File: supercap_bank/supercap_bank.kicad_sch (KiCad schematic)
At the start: 0 parts

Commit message: Update KiCad project files
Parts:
- added C20, C21, C22, C23: 10 F, capacitor_footprints:C_197x394_H31_5_5_0x10Metric, symbol CAPACITORS_HV_DATA_BASE:C_HV1030-2R7106-R
- added FID1, FID2, FID3: Fiducial, no_components_footprints:Fiducial_0.5mm_Mask1mm, symbol UNITED_NO_COMPONENTS_DATA_BASE:Fiducial
- added J10, J6, J7, J8, J9: FTSH-102-04-L-DH, connector_footprints:FTSH-102-04-L-DH, symbol CONNECTORS_FTSH-1xx-04-L-DH_DATA_BASE:J_FTSH-102-04-L-DH
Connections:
- new net GND: C23.2, J10.1, J10.2, J10.3, J10.4
- new net VCAP: C20.1, J6.1, J6.2, J6.3, J6.4
- new net VCAP_1: C22.2, C23.1, J9.1, J9.2, J9.3, J9.4
- new net VCAP_2: C21.2, C22.1, J8.1, J8.2, J8.3, J8.4
- new net VCAP_3: C20.2, C21.1, J7.1, J7.2, J7.3, J7.4

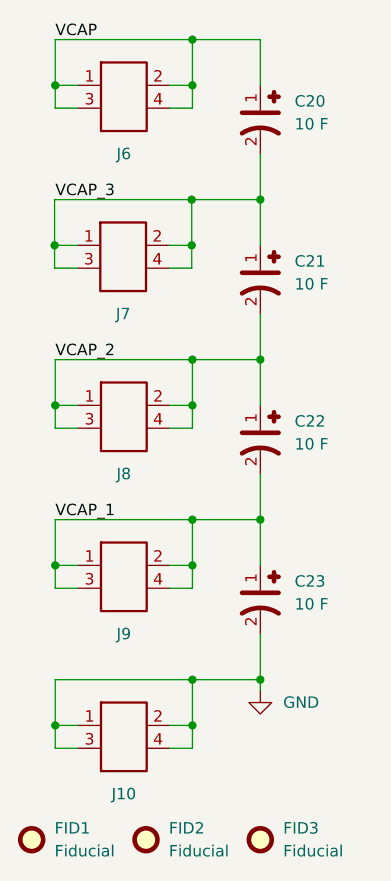
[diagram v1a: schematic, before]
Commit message: Update KiCAD configuration and project files
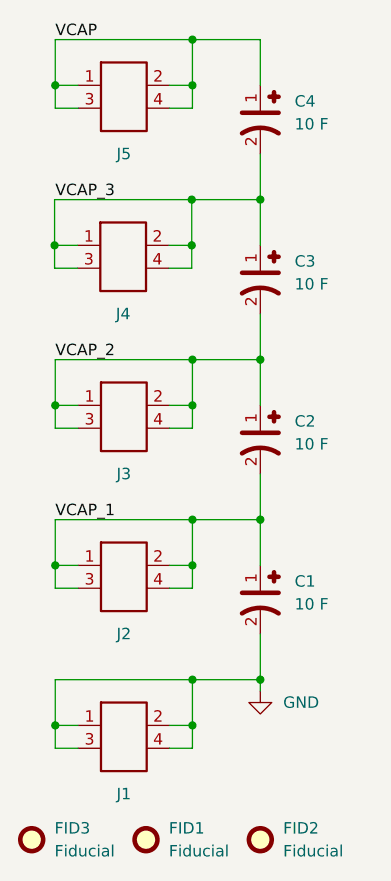
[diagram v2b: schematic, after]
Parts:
- renumbered C23 to C1, C22 to C2, C21 to C3, C20 to C4, FID2 to FID1, FID3 to FID2, FID1 to FID3, J10 to J1, J9 to J2, J8 to J3, J7 to J4, J6 to J5
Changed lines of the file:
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@@
 		(dnp no)
 		(fields_autoplaced yes)
-		(property "Reference" "J6"
+		(property "Reference" "J5"
 			(at 149.9365 58.42 0)
 			(effects
@@
 			(project ""
 				(path "/c896fba9-ce18-4c7c-9ca0-858a4c405263"
-					(reference "J6")
+					(reference "J5")
 					(unit 1)
 				)
@@
 		(dnp no)
 		(fields_autoplaced yes)
-		(property "Reference" "C23"
+		(property "Reference" "C1"
 			(at 168.91 105.9179 90)
 			(effects
@@
 			(project "supercap_bank"
 				(path "/c896fba9-ce18-4c7c-9ca0-858a4c405263"
-					(reference "C23")
+					(reference "C1")
 					(unit 1)
 				)
@@
 		(dnp no)
 		(fields_autoplaced yes)
-		(property "Reference" "FID2"
+		(property "Reference" "FID1"
 			(at 154.94 133.3499 0)
 			(effects
@@
 			(project "supercap_bank"
 				(path "/c896fba9-ce18-4c7c-9ca0-858a4c405263"
-					(reference "FID2")
+					(reference "FID1")
 					(unit 1)
 				)
@@
 		(dnp no)
 		(fields_autoplaced yes)
-		(property "Reference" "J10"
+		(property "Reference" "J1"
 			(at 149.9365 129.54 0)
 			(effects
@@
 			(project "supercap_bank"
 				(path "/c896fba9-ce18-4c7c-9ca0-858a4c405263"
-					(reference "J10")
+					(reference "J1")
 					(unit 1)
 				)
@@
 		(dnp no)
 		(fields_autoplaced yes)
-		(property "Reference" "C22"
+		(property "Reference" "C2"
 			(at 168.91 88.1379 90)
 			(effects
@@
 			(project "supercap_bank"
 				(path "/c896fba9-ce18-4c7c-9ca0-858a4c405263"
-					(reference "C22")
+					(reference "C2")
 					(unit 1)
 				)
@@
 		(dnp no)
 		(fields_autoplaced yes)
-		(property "Reference" "C21"
+		(property "Reference" "C3"
 			(at 168.91 70.3579 90)
 			(effects
@@
 			(project "supercap_bank"
 				(path "/c896fba9-ce18-4c7c-9ca0-858a4c405263"
-					(reference "C21")
+					(reference "C3")
 					(unit 1)
 				)
@@
 		(dnp no)
 		(fields_autoplaced yes)
-		(property "Reference" "J9"
+		(property "Reference" "J2"
 			(at 149.9365 111.76 0)
 			(effects
@@
 			(project "supercap_bank"
 				(path "/c896fba9-ce18-4c7c-9ca0-858a4c405263"
-					(reference "J9")
+					(reference "J2")
 					(unit 1)
 				)
@@
 		(dnp no)
 		(fields_autoplaced yes)
-		(property "Reference" "J7"
+		(property "Reference" "J4"
 			(at 149.86 76.2 0)
 			(effects
@@
 			(project "supercap_bank"
 				(path "/c896fba9-ce18-4c7c-9ca0-858a4c405263"
-					(reference "J7")
+					(reference "J4")
 					(unit 1)
 				)
@@
 		(dnp no)
 		(fields_autoplaced yes)
-		(property "Reference" "J8"
+		(property "Reference" "J3"
 			(at 149.9365 93.98 0)
 			(effects
@@
 			(project "supercap_bank"
 				(path "/c896fba9-ce18-4c7c-9ca0-858a4c405263"
-					(reference "J8")
+					(reference "J3")
 					(unit 1)
 				)
@@
 		(dnp no)
 		(fields_autoplaced yes)
-		(property "Reference" "C20"
+		(property "Reference" "C4"
 			(at 168.91 52.5779 90)
 			(effects
@@
 			(project "supercap_bank"
 				(path "/c896fba9-ce18-4c7c-9ca0-858a4c405263"
-					(reference "C20")
+					(reference "C4")
 					(unit 1)
 				)
@@
 		(dnp no)
 		(fields_autoplaced yes)
-		(property "Reference" "FID1"
+		(property "Reference" "FID3"
 			(at 142.24 133.3499 0)
 			(effects
@@
 			(project "supercap_bank"
 				(path "/c896fba9-ce18-4c7c-9ca0-858a4c405263"
-					(reference "FID1")
+					(reference "FID3")
 					(unit 1)
 				)
@@
 		(dnp no)
 		(fields_autoplaced yes)
-		(property "Reference" "FID3"
+		(property "Reference" "FID2"
 			(at 167.64 133.3499 0)
 			(effects
@@
 			(project "supercap_bank"
 				(path "/c896fba9-ce18-4c7c-9ca0-858a4c405263"
-					(reference "FID3")
+					(reference "FID2")
 					(unit 1)
 				)
